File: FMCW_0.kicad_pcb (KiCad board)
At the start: 6 copper layers, 100 x 100 mm, 311 parts, among them J1 Conn_02x07_Odd_Even, J2 HFJ11-1G41E-L12RL, J3 Conn_Coaxial_Small, J4 USB_C_Receptacle_USB2.0_16P, J5 Barrel_Jack_Switch, J6 USB_C_Receptacle_USB2.0_16P, J7 Conn_Coaxial_Small, J8 Conn_Coaxial_Small, SW1 SW_SPDT, SW2 SW_Push, SW3 SW_DIP_x04, SW4 SW_Push, U1 PAT1220-C-6DB, U10 LMX2491, U11 MAX275X, U12 5400BL15B050, U13 5400BL15B050, U14 ADL5380, U15 TPS259620, U16 Kria K24 SoM, U17 AP2127K-1.0, U18 AP2127K-2.5, U19 DP83867CRRGZR, U2 PAT1220-C-6DB, U20 SN74LVC2G06, U21 TPS53119, U22 TPS54308, U23 TPS54308, U24 CSD87352Q5D, U25 SN74LVC1G06, U26 TPS3839K33DBZR, U27 TPS3839G18DBZR, U28 AP22816AKEWT, U29 USB3300-EZK, U3 LMK1C1103A, U30 FT231XQ, U4 AP63200WU, U5 TLV76750QWDRBxQ1, U6 TLV76733QWDRBxQ1, U7 TPS3839K50DBZR, U8 TPS3839K33DBZR, U9 MCP3911, Y1 ECS-2520MV-160-BN, Y2 25MHz, Y3 ECS-240-12-37B-CKY-TR

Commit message: some changes. layout routing done. need to check eth/usb length matching
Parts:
- U15: footprint Package_SO:TI_SO-PowerPAD-8_ThermalVias -> Package_SO:TI_SO-PowerPAD-8
- U21: footprint Package_DFN_QFN:VQFN-16-1EP_3x3mm_P0.5mm_EP1.45x1.45mm_ThermalVias -> Package_DFN_QFN:VQFN-16-1EP_3x3mm_P0.5mm_EP1.45x1.45mm
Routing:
- net GND: track 150.6 -> 168.0 mm, vias 277 -> 333
- net Net-(U28-OUT): track 18.2 -> 26.0 mm
- net /RFFE/ADC/adc_dvdd: track 3.58 -> 10.2 mm
- net +3.3VA: track 13.1 -> 16.0 mm, vias 6 -> 9
- net Net-(U14-ENBL): track 0.00 -> 1.91 mm
- net Net-(RN3C-R3.1): track 2.32 -> 4.07 mm
- net Net-(C39-Pad1): track 0.00 -> 1.28 mm
- net Net-(C38-Pad1): track 0.00 -> 1.28 mm
- net Net-(U14-LOIN): track 0.00 -> 1.24 mm
- net Net-(U14-LOIP): track 0.00 -> 1.24 mm

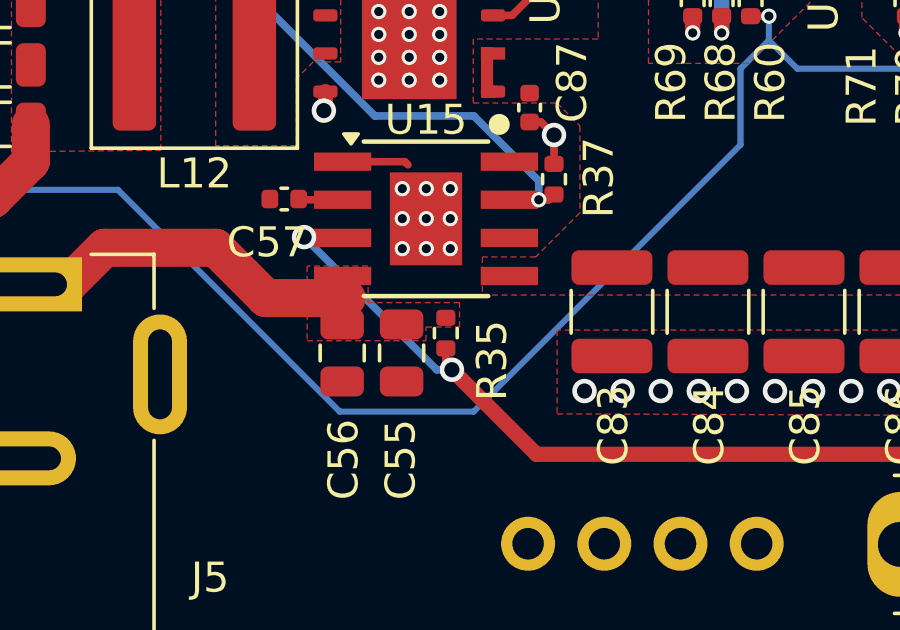
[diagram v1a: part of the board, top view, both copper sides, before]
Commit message: added resistor divider to efuse. add k24 datasheet
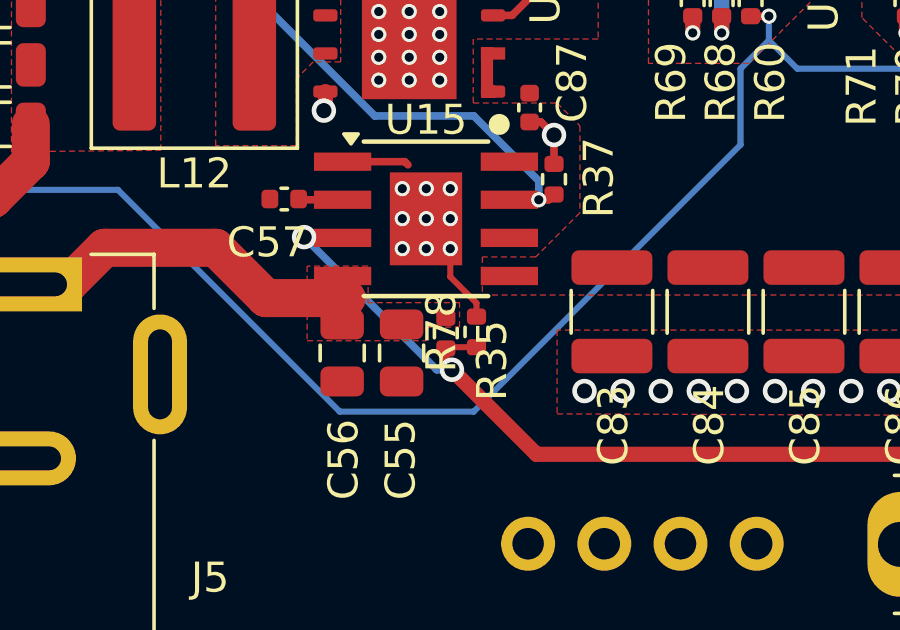
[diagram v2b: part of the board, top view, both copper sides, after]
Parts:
- added R78: 22k, Resistor_SMD:R_0402_1005Metric, F.Cu at (140.8, 124.8)
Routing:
- net GND: track 168.0 -> 170.6 mm
- net Net-(SW1-A): track 29.8 -> 30.8 mm

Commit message: Imon Schematic and DRC checking changes -Added current monitor ADC for Imon -Fixed unconnected nets -Added shorting resistor between both output power on signals from Kria SoM
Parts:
- added C26: 2.2u, Capacitor_SMD:C_0402_1005Metric, F.Cu at (161.6, 39.6)
- added C30: 100n, Capacitor_SMD:C_0402_1005Metric, F.Cu at (128.4, 103.6)
- added C32: 100n, Capacitor_SMD:C_0402_1005Metric, F.Cu at (134.0, 106.0)
- added R100: 4.7k, Resistor_SMD:R_0402_1005Metric, F.Cu at (134.0, 105.0)
- added R101: 0, Resistor_SMD:R_0402_1005Metric, F.Cu at (108.5, 96.5)
- added R99: 4.7k, Resistor_SMD:R_0402_1005Metric, F.Cu at (134.0, 104.0)
- added U31: MCP3221, Package_TO_SOT_SMD:SOT-23-5, F.Cu at (130.9, 104.1)
- moved C58 1.20 mm to (132.3, 107.0), turned to -90 degrees
- moved R38 1.17 mm to (131.3, 107.0), turned to 90 degrees
- moved C57 0.23 mm to (134.1, 120.3)
- moved R37 0.22 mm to (143.6, 119.7)
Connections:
- U16 pad JA_C22: unconnected-(U16JA_CD-HDA_18-PadJA_C22) -> /fpga/fpga_ja/i2c_33_scl
- U16 pad JA_C23: unconnected-(U16JA_CD-HDA_19-PadJA_C23) -> /fpga/fpga_ja/i2c_33_sda
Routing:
- net /fpga/fpga_ja/i2c_33_sda: track 0.00 -> 29.4 mm, vias 0 -> 2
- net GND: track 170.6 -> 198.2 mm, vias 333 -> 359
- net /fpga/fpga_ja/i2c_33_scl: track 0.00 -> 27.1 mm, vias 0 -> 2
- net +3V3: track 110.9 -> 118.7 mm, vias 17 -> 19
- net Net-(J4-VBUS-PadA4): track 3.80 -> 9.83 mm
- net /efuse/Imon: track 0.00 -> 3.07 mm
- net /fpga/fpga_ja/PS_SUPPLY_START: track 0.00 -> 1.75 mm
- net Net-(J1-Pin_12): track 72.2 -> 72.9 mm
- net Net-(J1-Pin_10): track 66.5 -> 67.1 mm
- net /RFFE/rffe_ps_en: track 164.9 -> 165.5 mm
- net Net-(J1-Pin_6): track 66.0 -> 66.5 mm
- net /fpga/fpga_ja/PS_SRST_N: track 76.6 -> 76.5 mm, vias 2 -> 1

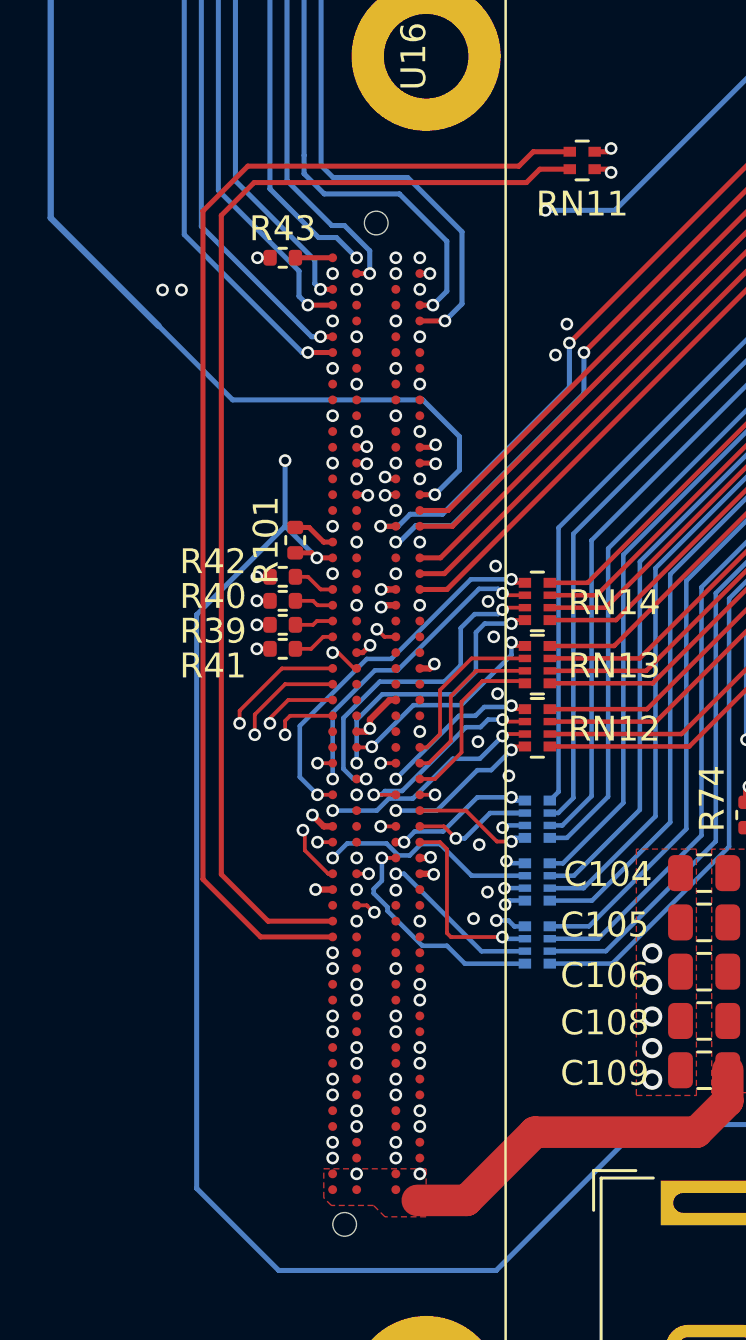
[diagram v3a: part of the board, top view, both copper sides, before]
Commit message: Layout Updates -changed power sequence resistor connections
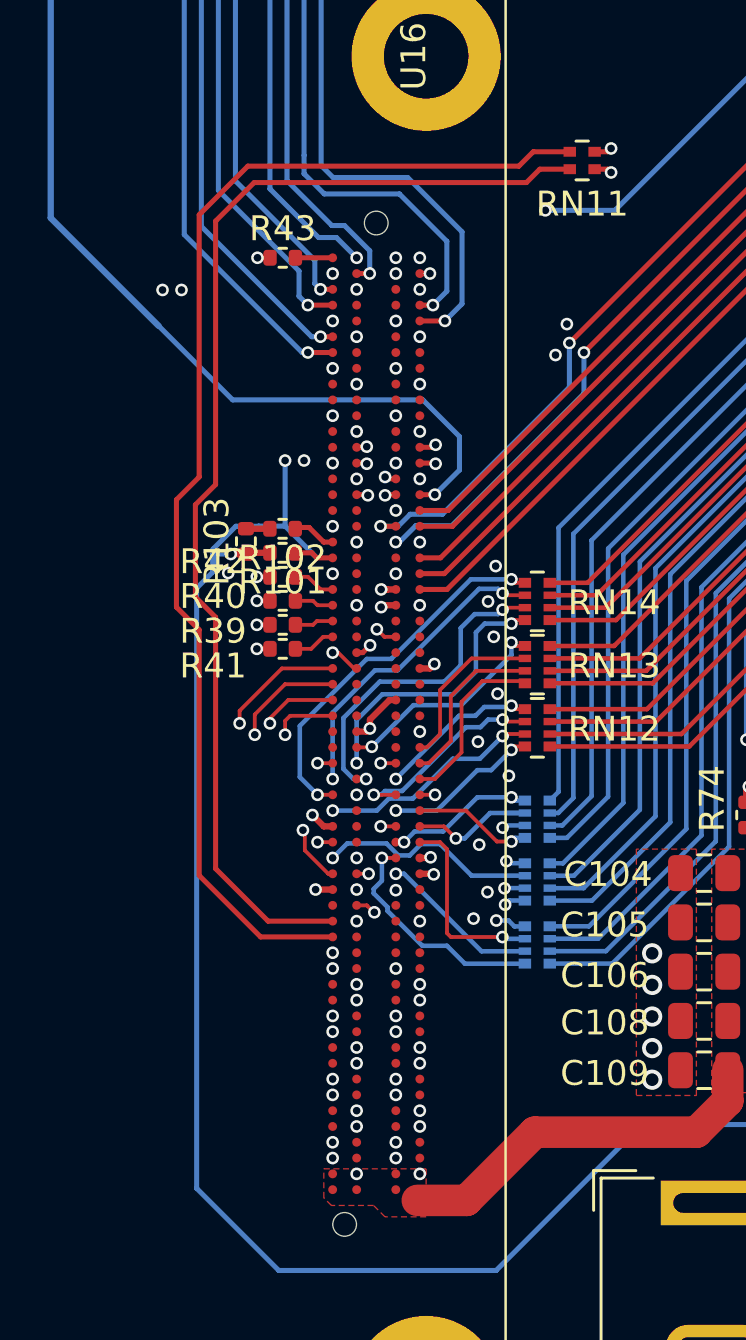
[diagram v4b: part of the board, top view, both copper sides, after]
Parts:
- added R102: 0, Resistor_SMD:R_0402_1005Metric, F.Cu at (108.0, 96.1)
- added R103: DNI, Resistor_SMD:R_0402_1005Metric, F.Cu at (106.5, 96.6)
- moved R101 0.72 mm to (108.0, 97.1), turned to 180 degrees
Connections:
- R101 pad 1: /RFFE/rffe_ps_en -> Net-(U16JA_AB-VCCOEN_PL_M2C)
- R101 pad 2: /fpga/fpga_ja/PS_SUPPLY_START -> /RFFE/rffe_ps_en
- U16 pad JA_A19: /fpga/fpga_ja/PS_SUPPLY_START -> Net-(U16JA_AB-VCCOEN_PS_M2C)
- U16 pad JA_A20: /RFFE/rffe_ps_en -> Net-(U16JA_AB-VCCOEN_PL_M2C)
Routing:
- net /RFFE/rffe_ps_en: track 165.5 -> 168.1 mm
- net Net-(U16JA_AB-VCCOEN_PS_M2C): track 0.00 -> 1.75 mm
- net Net-(U16JA_AB-VCCOEN_PL_M2C): track 0.00 -> 1.59 mm
- net /fpga/fpga_ja/uart_txd: track 48.8 -> 49.7 mm
- net /fpga/fpga_ja/uart_rxd: track 46.5 -> 47.4 mm
- net /fpga/fpga_ja/PS_SUPPLY_START: track 1.75 -> 0.96 mm
- net GND: vias 359 -> 361
